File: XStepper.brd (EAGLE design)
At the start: 100.3 x 80 mm, 69 parts, among them IC1 LM7805, Q2 16 MHZ

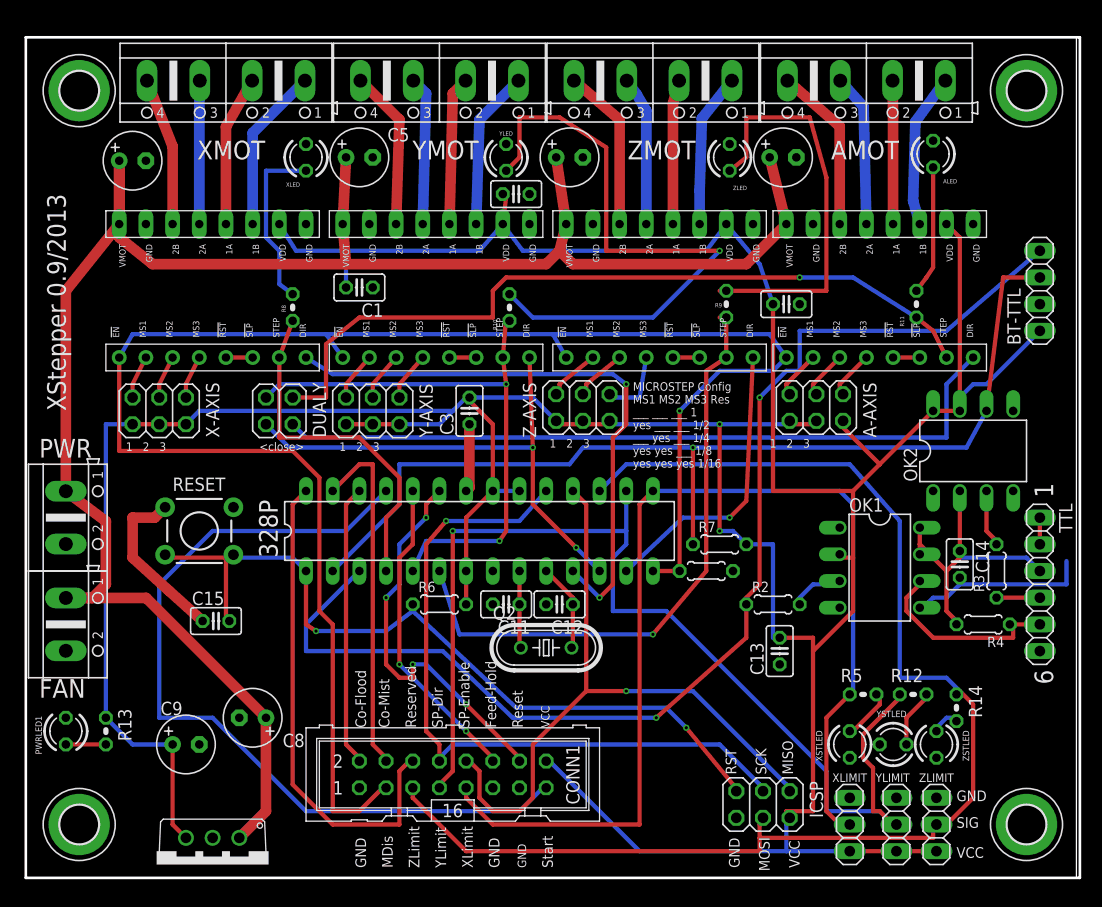
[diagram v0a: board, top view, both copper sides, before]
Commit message: add pullup resistors for Hallo Sensor switches (Cherry MP101401)
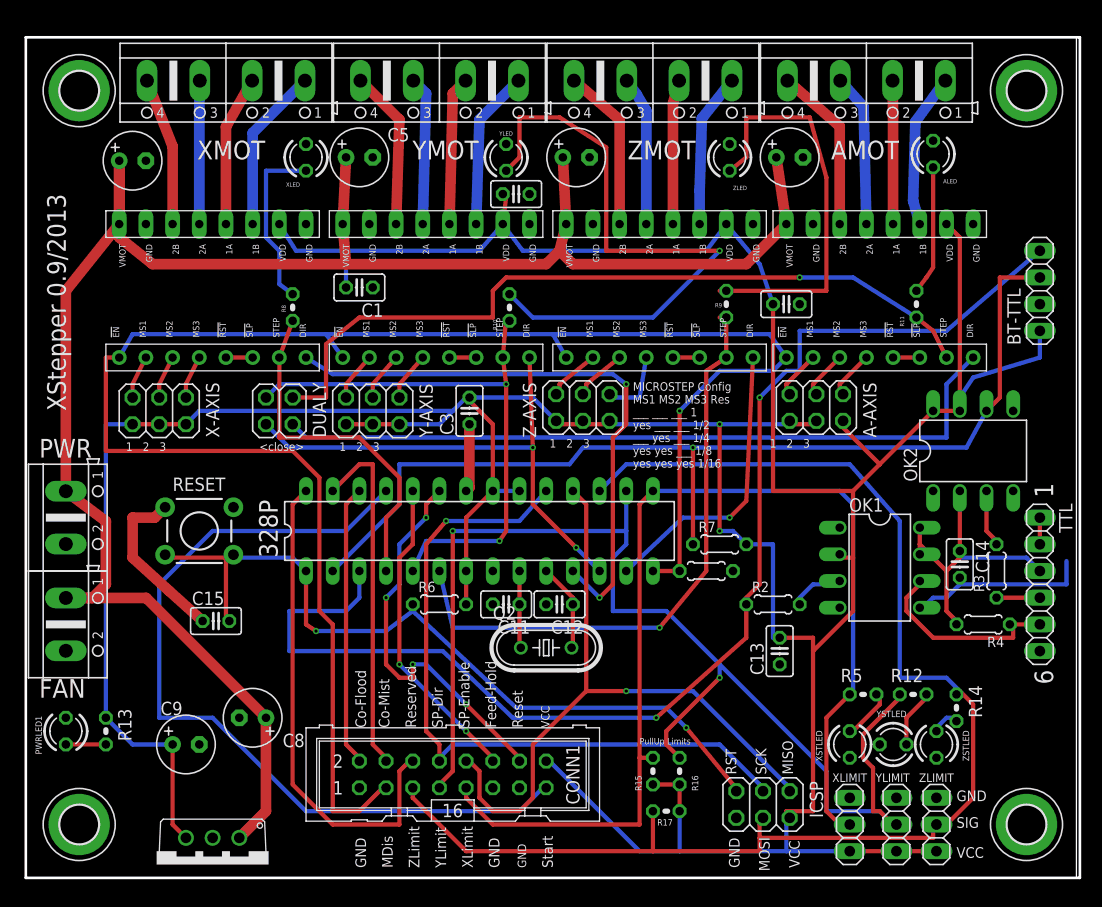
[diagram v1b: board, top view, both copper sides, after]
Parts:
- added R15, R16, R17: 1k, resistor:0204V
- moved C7 0.64 mm to (52.4, 68.6)
- moved C10 0.63 mm to (72.7, 68.6)
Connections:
- net 5V: now also R15.1, R16.1, R17.1
- net X-STOP: now also R15.2
- net Y-STOP: now also R16.2
- net Z-STOP: now also R17.2
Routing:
- net Y-STOP: track 106.8 -> 118.5 mm, vias 1 -> 2
- net 5V: track 401.2 -> 411.3 mm
- net TXD: track 114.8 -> 120.2 mm
- net Z-STOP: track 127.1 -> 130.9 mm
- net MOTOR_DISABLE: track 169.0 -> 171.5 mm
- net X-STOP: track 104.1 -> 105.4 mm
- net RXD: track 97.0 -> 97.8 mm
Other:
- board text added: "PullUp Limits"

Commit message: Bugfree version from 0.9 to produce in ITEAD
Version 0.91 from Matt to produce without bugs
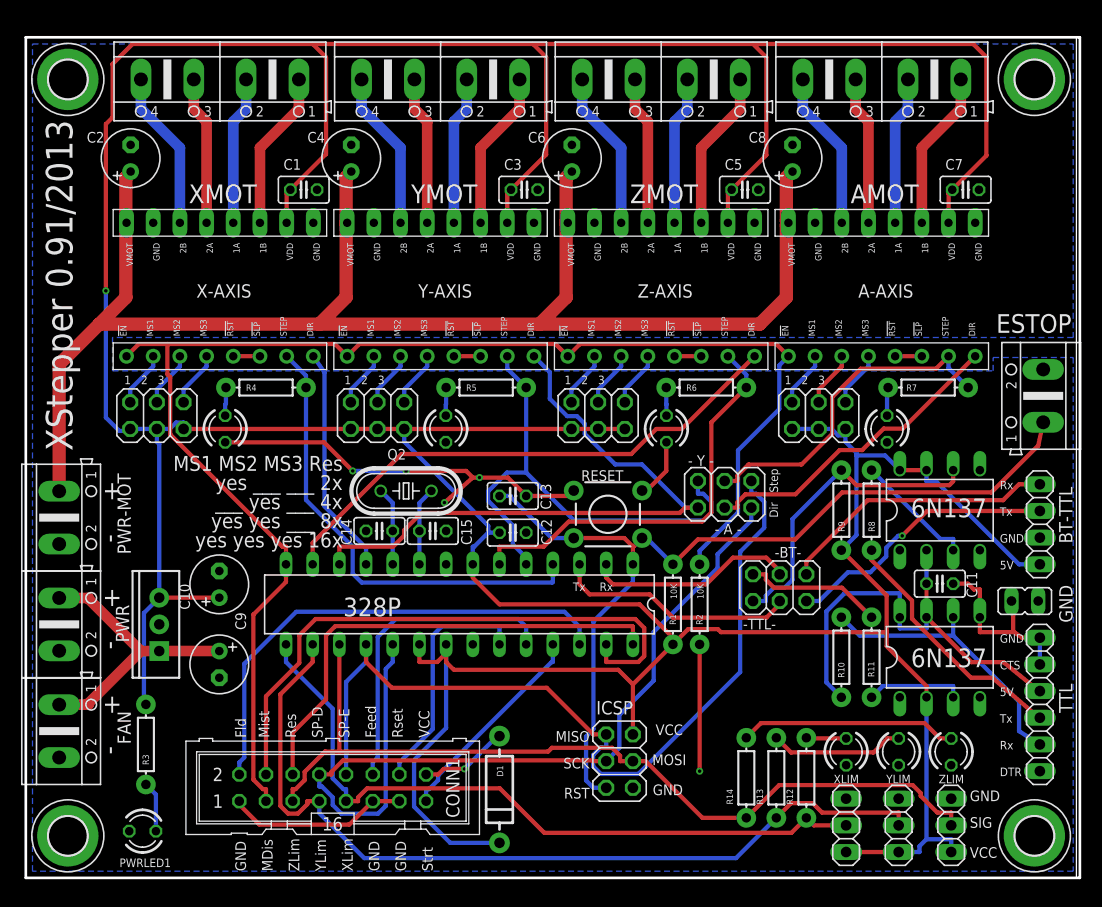
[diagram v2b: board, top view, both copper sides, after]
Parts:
- removed DUALY: (no value), pinhead:2X02
- removed R15, R16, R17: 1k, resistor:0204V
- removed XLIMIT, YLIMIT, ZLIMIT: (no value), pinhead:1X03
- added COMMSEL, JP1: (no value), pinhead:2X03
- added D1: (no value), SparkFun-DiscreteSemi:DIODE-1N4001
- added ESTOP, PWR-MOT: (no value), con-ptr500:AK500/2
- added GND: (no value), jumper:JP1
- added XLIM, YLIM, ZLIM: (no value), pinhead:1X03
- C11, C12: value 18pF -> 0.1uF
- C14, C15: value 0.1uF -> 18pF
- C2, C8: value 47uF -> 100uF
- C4, C6: value 0.1uF -> 100uF; device resistor:C025-025X050 -> resistor:E2,5-6
- C5, C7: value 47uF -> 0.1uF; device resistor:E2,5-6 -> resistor:C025-025X050
- C9: value 47uF -> 200uF
- IC1: value LM7805 -> (none); device SparkFun:78XXL-CUSTOM -> SparkFun-PowerIC:TO220-IGO
- R1: value 10k -> 10K; device resistor:0204/5 -> SparkFun-Resistors:AXIAL-0.3
- R10, R11, R12, R14, R5, R8, R9: value 470 -> (none); device resistor:0204V -> SparkFun-Resistors:AXIAL-0.3
- R13: value 1k -> (none); device resistor:0204V -> SparkFun-Resistors:AXIAL-0.3
- R2: value 470 -> 10K; device resistor:0204/5 -> SparkFun-Resistors:AXIAL-0.3
- R3, R4, R7: value 470 -> (none); device resistor:0204/5 -> SparkFun-Resistors:AXIAL-0.3
- R6: value 10k -> (none); device resistor:0204/5 -> SparkFun-Resistors:AXIAL-0.3
- moved R3 82.6 mm to (11.4, 12.7), turned to 270 degrees
- moved C8 74.0 mm to (73.0, 68.5), turned to 90 degrees
- moved R4 71.9 mm to (22.9, 46.7), turned to 0 degrees
- moved C10 67.8 mm to (18.4, 27.9), turned to 90 degrees
- moved R13 64.0 mm to (71.4, 9.53), turned to 90 degrees
- moved R8 58.4 mm to (80.5, 35.0)
- moved C14 55.3 mm to (33.7, 33.0), turned to 180 degrees
- moved R5 46.3 mm to (43.8, 46.7)
- moved R10 45.9 mm to (77.6, 21.0), turned to 270 degrees
- moved C11 41.3 mm to (87.0, 28.0), turned to 0 degrees
- moved RESET 38.9 mm to (55.4, 34.6)
- moved C7 37.2 mm to (89.5, 65.5), turned to 180 degrees
- moved C5 36.8 mm to (68.5, 65.5), turned to 180 degrees
- moved R11 33.9 mm to (80.5, 21.0)
- moved R6 32.7 mm to (64.8, 46.7)
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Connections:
- removed net GNDA: C14.2, OK1.5
- new net BTRXD: BT-TTL.3, COMMSEL.5
- new net BTTXD: BT-TTL.4, COMMSEL.6
- new net N$45: CONN1.16, D1.A
- new net PWRMOT: C2.+, C4.+, C6.+, C8.+, PWR-MOT.1, STEPPERDRIVER.VMOT, STEPPERDRIVER1.VMOT, STEPPERDRIVER2.VMOT, STEPPERDRIVER3.VMOT
- new net RXDUSB: COMMSEL.1, OK2.6, R9.P$2
- new net TXDUSB: COMMSEL.2, R11.P$2
- new net USB_GND: C11.2, GND.1, OK1.5, TTL.1, TTL.2
- net 12V: now also C9.+; no longer C10.+, C2.+, C5.+, C7.+, C8.+, STEPPERDRIVER.VMOT, STEPPERDRIVER1.VMOT, STEPPERDRIVER2.VMOT, STEPPERDRIVER3.VMOT
- net 5V: now also C10.+, C12.2, C5.2, C7.2, D1.C, R1.P$2, R3.P$1, R9.P$1, XLIM.1, YLIM.1, ZLIM.1; no longer C13.2, C4.2, C6.2, C9.+, CONN1.16, R13.1, R15.1, R16.1, R17.1, R6.2, R7.2, XLIMIT.1, YLIMIT.1, ZLIMIT.1
- net A-DIR: now also JP1.4; no longer DUALY.2
- net A-STEP: now also JP1.3, R7.P$2; no longer DUALY.1, R11.1
- net GND: now also C12.1, C14.2, C15.2, C4.-, C5.1, C6.-, C7.1, ESTOP.2, GND.2, PWR-MOT.2, R2.P$2, XLIM.3, YLIM.3, ZLIM.3; no longer C11.2, C12.2, C15.1, C4.1, C5.-, C6.1, C7.-, R1.1, TTL.1, TTL.2, XLIMIT.3, YLIMIT.3, ZLIMIT.3
- net MOTOR_DISABLE: now also R2.P$1; no longer R1.2
- net N$33: now also C15.1; no longer C11.1
- net N$34: now also C14.1; no longer C12.1
- net N$35: now also R8.P$2; no longer R3.2
- net N$36: now also R11.P$1; no longer R2.2
- net N$37: now also R12.P$2; no longer R5.2
- net N$38: now also R4.P$1; no longer R8.2
- net N$39: now also R5.P$1, YLED.A; no longer R9.2, ZLED.A
- net N$40: now also R6.P$1, ZLED.A; no longer R10.2, YLED.A
- net N$41: now also R7.P$1; no longer R11.2
- net N$42: now also R13.P$2; no longer R12.2
- net N$43: now also R3.P$2; no longer R13.2
- net N$44: now also R14.P$2; no longer R14.2
- net RESET: now also C13.2, ESTOP.1, R1.P$1; no longer C15.2, R6.1
- net RXD: now also COMMSEL.4; no longer BT-TTL.3, OK2.6, R7.1
- net SPINDLE-DIR: now also JP1.2
- net SPINDLE-ENABLE: now also JP1.1
- net TXD: now also COMMSEL.3; no longer BT-TTL.4, R2.1
- net USB_5V: now also C11.1, R10.P$2; no longer C14.1, R4.2
- net USB_RXD: now also R10.P$1; no longer R4.1
- net USB_TXD: now also R8.P$1; no longer R3.1
- net X-STEP: now also R4.P$2; no longer R8.1
- net X-STOP: now also R12.P$1, XLIM.2; no longer R15.2, R5.1, XLIMIT.2
- net Y-DIR: now also JP1.6; no longer DUALY.4
- net Y-STEP: now also JP1.5, R5.P$2; no longer DUALY.3, R10.1
- net Y-STOP: now also R13.P$1, YLIM.2; no longer R12.1, R16.2, YLIMIT.2
- net Z-STEP: now also R6.P$2; no longer R9.1
- net Z-STOP: now also R14.P$1, ZLIM.2; no longer R14.1, R17.2, ZLIMIT.2
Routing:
- net 12V: track 184.5 -> 27.3 mm
- net PWRMOT: track 0.00 -> 144.0 mm
- net TXD: track 120.2 -> 23.1 mm, vias 2 -> 0
- net RXD: track 97.8 -> 19.9 mm, vias 1 -> 0
- net 5V: track 411.3 -> 483.4 mm, vias 2 -> 1
- net CYCLE-START: track 79.9 -> 20.2 mm
- net N$40: track 59.3 -> 2.68 mm, vias 1 -> 0
- net GND: track 26.3 -> 74.4 mm, vias 0 -> 5
- net Z-STOP: track 130.9 -> 82.9 mm
- net A-STEP: track 74.4 -> 32.3 mm, vias 1 -> 0
- net A-DIR: track 71.4 -> 30.1 mm
- net X-STOP: track 105.4 -> 68.4 mm
- net N$39: track 38.8 -> 2.68 mm
- net Y-STOP: track 118.5 -> 83.1 mm, vias 2 -> 0
- net X-DIR: track 56.2 -> 21.8 mm, vias 2 -> 0
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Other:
- board text added: "+"
- board text added: "-"
- board text added: "- A -"
- board text added: "- Y -"
- board text added: "-BT-"
- board text added: "-TTL-"
- board text added: "5V"
- board text added: "6N137"
- board text added: "C6"
- board text added: "C8"
- board text added: "CTS"
- board text added: "DTR"
- board text added: "Dir"
- board text added: "Feed"
- board text added: "Fld"
- board text added: "MS1 MS2 MS3 Res yes ___ ___ 2x ___ yes ___ 4x yes yes ___ 8x yes yes yes 16x"
- board text added: "Mist"
- board text added: "Res"
- board text added: "Rset"
- board text added: "Rx"
- board text added: "SP-D"
- board text added: "SP-E"
- board text added: "Step"
- board text added: "Strt"
- board text added: "Tx"
- board text added: "XLim"
- board text added: "XStepper 0.91/2013"
- board text added: "YLim"
- board text added: "ZLim"
- board text removed: "1"
- board text removed: "6"
- board text removed: "<close>"
- board text removed: "Co-Flood"
- board text removed: "Co-Mist"
- board text removed: "Feed-Hold"
- board text removed: "MICROSTEP Config MS1 MS2 MS3 Res ___ ___ ___ 1 yes ___ ___ 1/2 ___ yes ___ 1/4 yes yes ___ 1/8 yes yes yes 1/16"
- board text removed: "PullUp Limits"
- board text removed: "Reserved"
- board text removed: "Reset"
- board text removed: "SP-Dir"
- board text removed: "SP-Enable"
- board text removed: "Start"
- board text removed: "XLimit"
- board text removed: "XStepper 0.9/2013"
- board text removed: "YLimit"
- board text removed: "ZLimit"

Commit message: - change header ICSP
- more space between caps at 7805
- add VCC area on top to save wires
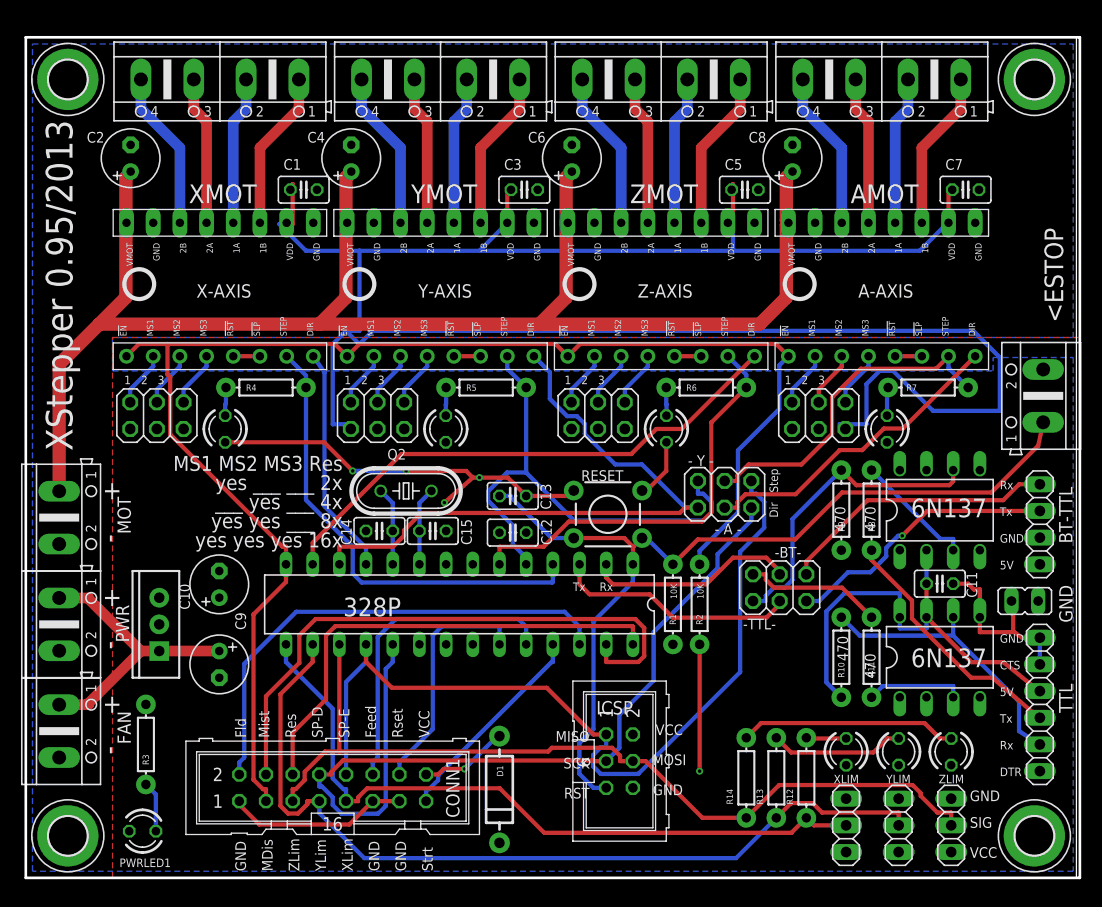
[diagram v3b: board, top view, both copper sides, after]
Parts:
- C10: value 47uF -> 100uF
- ICSP: device pinhead:2X03 -> con-ml:ML6
- R10, R11, R8, R9: value (none) -> 470
- renumbered ESTOP to <ESTOP, PWR-MOT to MOT
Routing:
- net 5V: track 483.4 -> 201.2 mm, vias 1 -> 0
- net RESET: track 88.0 -> 88.5 mm
- added copper zone on layer 1, net 5V
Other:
- board text added: "XStepper 0.95/2013"
- board text removed: "XStepper 0.91/2013"

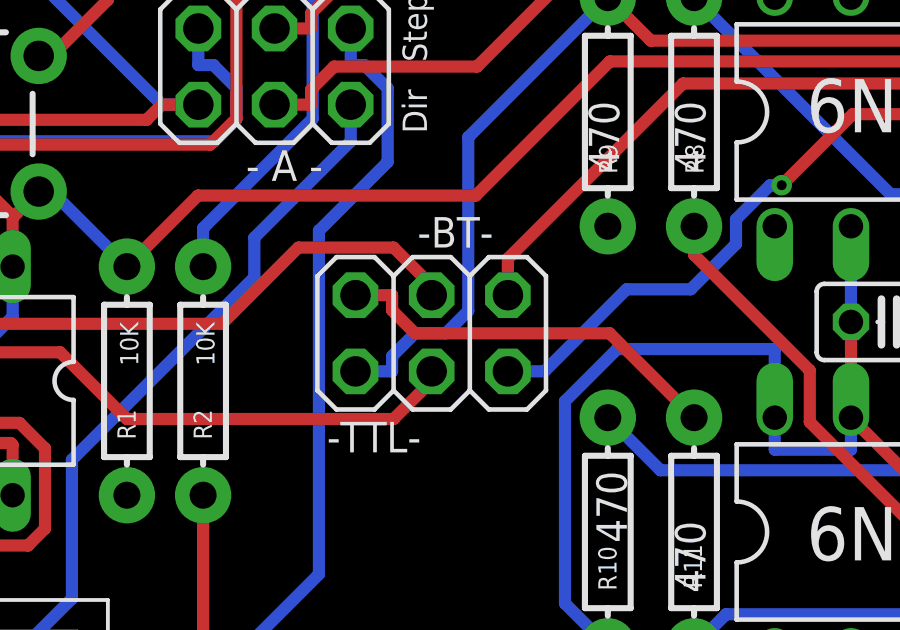
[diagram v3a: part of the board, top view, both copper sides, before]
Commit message: - Bugfix COMSERIAL
change pins on comserial block
remove some unused files
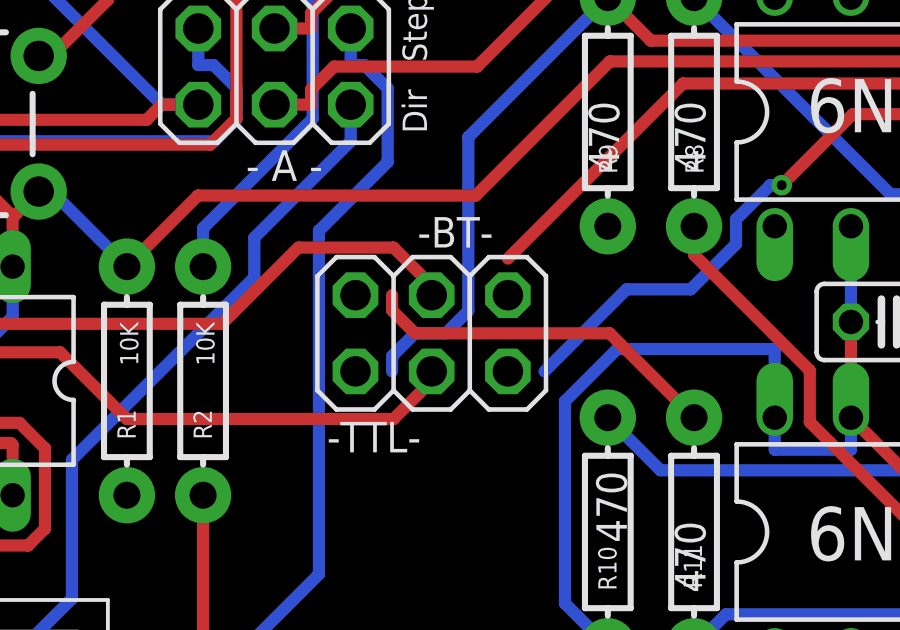
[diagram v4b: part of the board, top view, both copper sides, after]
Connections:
- net BTRXD: now also COMMSEL.6; no longer COMMSEL.5
- net BTTXD: now also COMMSEL.5; no longer COMMSEL.6
- net RXDUSB: now also COMMSEL.2; no longer COMMSEL.1
- net TXDUSB: now also COMMSEL.1; no longer COMMSEL.2
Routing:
- net BTRXD: track 26.3 -> 25.0 mm
- net BTTXD: track 26.5 -> 25.3 mm
- net TXDUSB: track 13.3 -> 12.1 mm
- net RXDUSB: track 29.7 -> 28.5 mm
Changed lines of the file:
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@@
 <signal name="BTTXD">
 <contactref element="BT-TTL" pad="4"/>
-<contactref element="COMMSEL" pad="6"/>
 <wire x1="96.52" y1="37.465" x2="94.5387" y2="37.465" width="0.4064" layer="1"/>
-<wire x1="74.295" y1="28.8925" x2="74.295" y2="30.1118" width="0.4064" layer="1"/>
 <wire x1="74.295" y1="30.1118" x2="80.132" y2="35.9488" width="0.4064" layer="1"/>
 <wire x1="80.132" y1="35.9488" x2="93.0225" y2="35.9488" width="0.4064" layer="1"/>
 <wire x1="93.0225" y1="35.9488" x2="94.5387" y2="37.465" width="0.4064" layer="1"/>
+<contactref element="COMMSEL" pad="5"/>
+<wire x1="74.295" y1="26.3525" x2="74.295" y2="30.1118" width="0" layer="19" extent="1-1"/>
 </signal>
 <signal name="BTRXD">
 <contactref element="BT-TTL" pad="3"/>
-<contactref element="COMMSEL" pad="5"/>
-<wire x1="74.295" y1="26.3525" x2="75.5143" y2="26.3525" width="0.4064" layer="16"/>
 <wire x1="83.4213" y1="32.5583" x2="85.788" y2="34.925" width="0.4064" layer="1"/>
 <wire x1="85.788" y1="34.925" x2="96.52" y2="34.925" width="0.4064" layer="1"/>
@@
 <wire x1="81.8972" y1="31.4164" x2="83.0391" y2="32.5583" width="0.4064" layer="16"/>
 <wire x1="83.0391" y1="32.5583" x2="83.4213" y2="32.5583" width="0.4064" layer="16"/>
+<contactref element="COMMSEL" pad="6"/>
+<wire x1="75.5143" y1="26.3525" x2="74.295" y2="28.8925" width="0" layer="19" extent="16-16"/>
 </signal>
 <signal name="TXDUSB">
 <contactref element="R11" pad="P$2"/>
-<contactref element="COMMSEL" pad="2"/>
-<wire x1="69.215" y1="28.8925" x2="70.4343" y2="28.8925" width="0.4064" layer="1"/>
 <wire x1="80.5" y1="24.81" x2="77.6875" y2="27.6225" width="0.4064" layer="1"/>
 <wire x1="77.6875" y1="27.6225" x2="71.1991" y2="27.6225" width="0.4064" layer="1"/>
 <wire x1="71.1991" y1="27.6225" x2="70.4343" y2="28.3873" width="0.4064" layer="1"/>
 <wire x1="70.4343" y1="28.3873" x2="70.4343" y2="28.8925" width="0.4064" layer="1"/>
+<contactref element="COMMSEL" pad="1"/>
+<wire x1="69.215" y1="26.3525" x2="71.1991" y2="27.6225" width="0" layer="19" extent="1-1"/>
 </signal>
 <signal name="RXDUSB">
 <contactref element="OK2" pad="6"/>
 <contactref element="R9" pad="P$2"/>
-<contactref element="COMMSEL" pad="1"/>
-<wire x1="69.215" y1="26.3525" x2="70.4343" y2="26.3525" width="0.4064" layer="16"/>
 <wire x1="77.625" y1="38.81" x2="72.9744" y2="34.1594" width="0.4064" layer="16"/>
 <wire x1="72.9744" y1="34.1594" x2="72.9744" y2="28.3686" width="0.4064" layer="16"/>
@@
 <wire x1="79.0589" y1="37.3761" x2="87.903" y2="37.3761" width="0.4064" layer="1"/>
 <wire x1="87.903" y1="37.3761" x2="88.27" y2="37.7431" width="0.4064" layer="1"/>
+<contactref element="COMMSEL" pad="2"/>
+<wire x1="71.1991" y1="27.6225" x2="69.215" y2="28.8925" width="0" layer="19" extent="16-16"/>
 </signal>
 <signal name="USB_GND" class="1">
